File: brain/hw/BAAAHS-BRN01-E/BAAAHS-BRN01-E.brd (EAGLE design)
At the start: 137.2 x 38.1 mm, 118 parts, among them J2 PINHD1X3-20AWG, J3 PINHD1X3-20AWG, J4 PINHD1X10-1X10, J7 PINHD1X2-1X02, Q1 MMBT3904, Q2 MMBT3904, U1 SN74LVC1T45-DCK6, U2 ESP32, U3 CH340T, U4 5V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

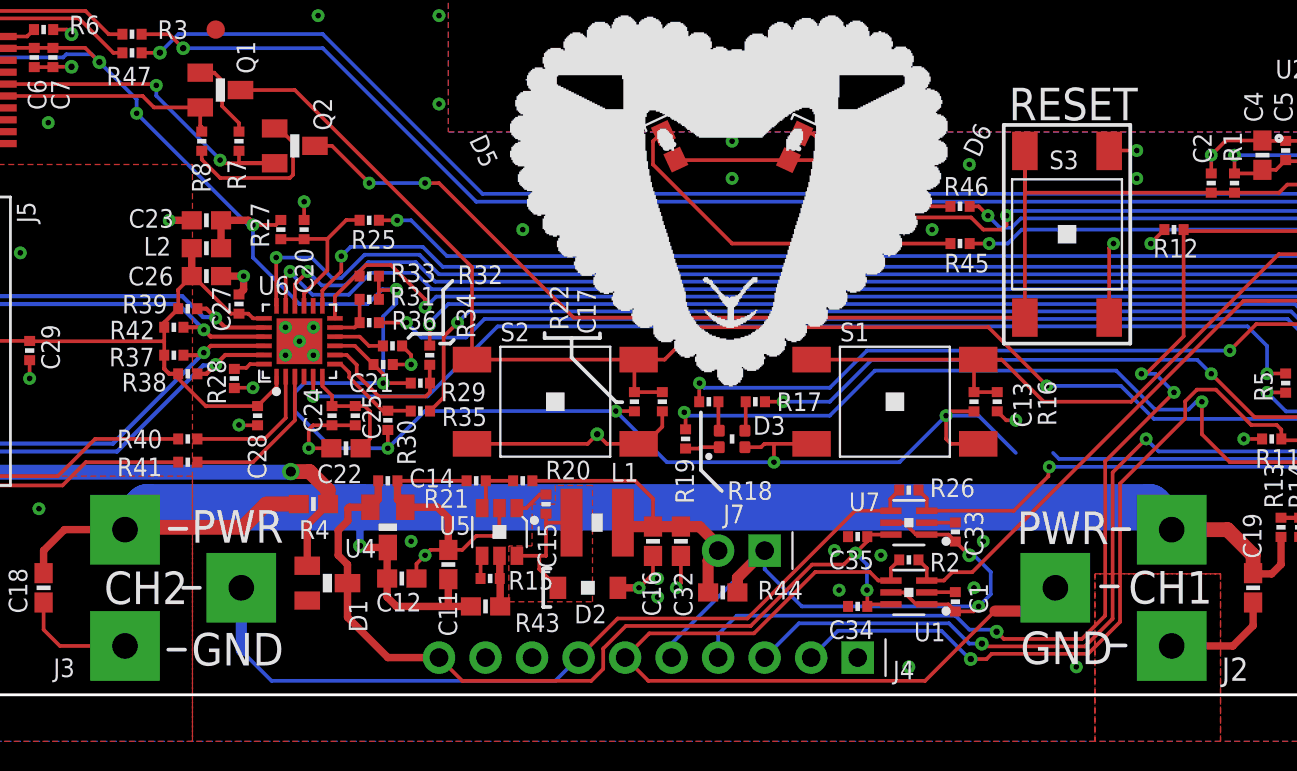
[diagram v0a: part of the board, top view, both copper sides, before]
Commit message: Updated Brain Controller Rev E files
Reflects feedback from Tom
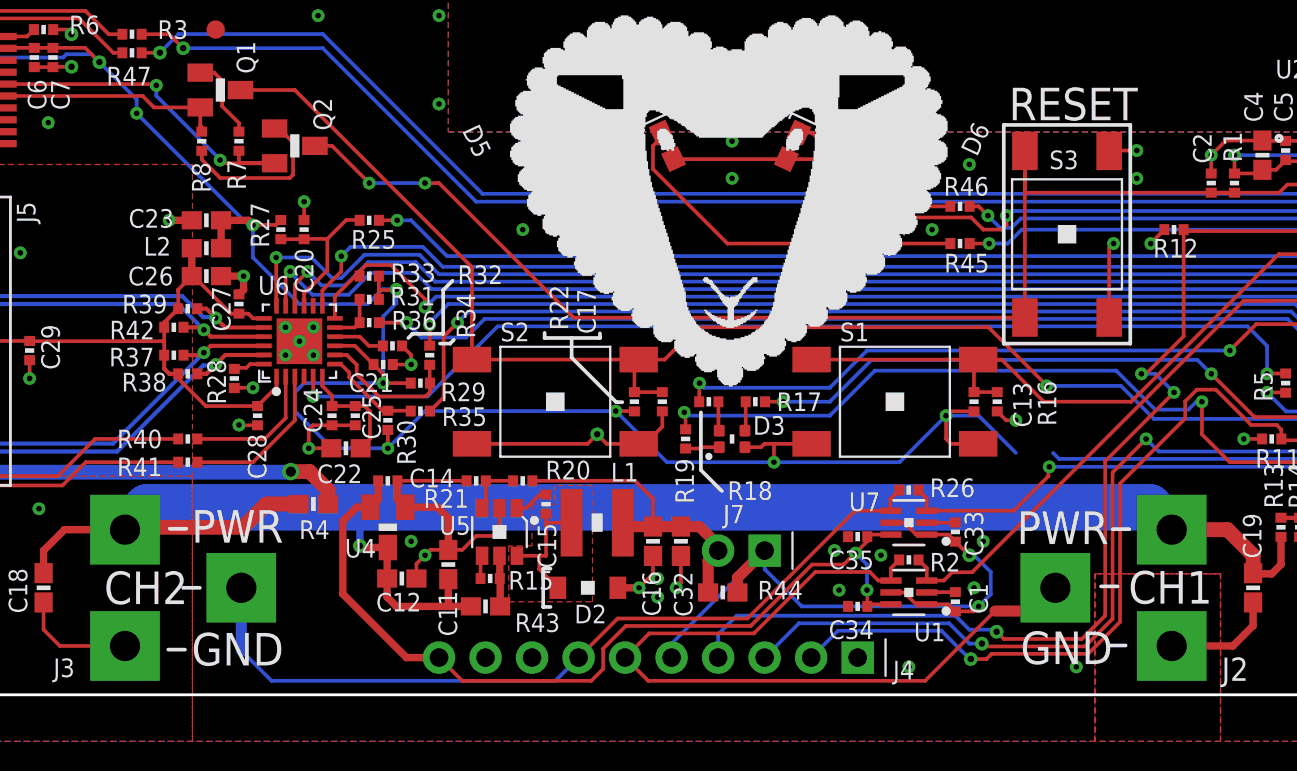
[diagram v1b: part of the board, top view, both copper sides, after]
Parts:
- removed D1: BAT54L, diodes:SOT23
- moved D6 0.13 mm to (76.5, 30.0)
- moved D5 0.12 mm to (69.6, 30.0)
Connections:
- net 5V0: no longer D1.3
- net VBUS: no longer D1.1
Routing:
- net VBUS: track 70.8 -> 67.0 mm
- net 5V0: track 49.5 -> 48.5 mm

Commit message: Updated Rev E Brain hardware files
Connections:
- net IO39_3V3IO_1_LOW renamed IO39_3V3IO_1_DOWN
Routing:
- net GND: track 568.3 -> 530.4 mm, vias 69 -> 75
